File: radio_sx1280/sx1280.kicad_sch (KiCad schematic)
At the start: 5 parts

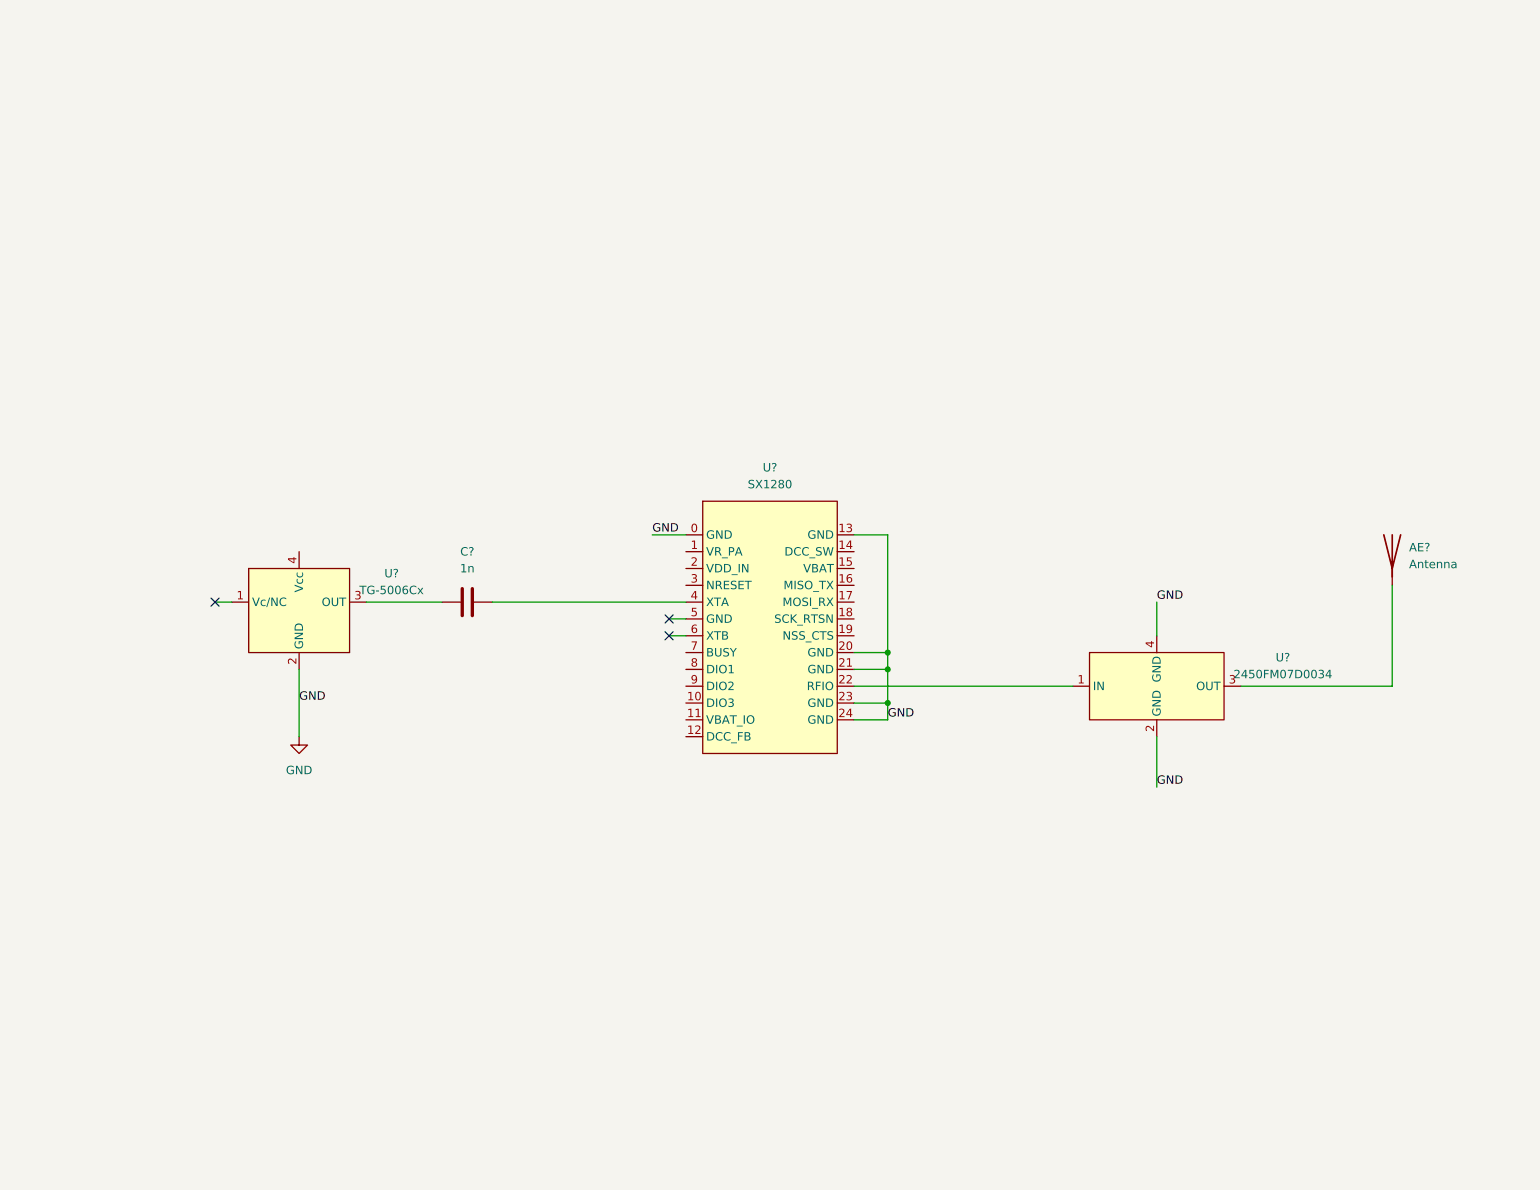
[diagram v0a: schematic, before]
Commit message: schematic capture complete
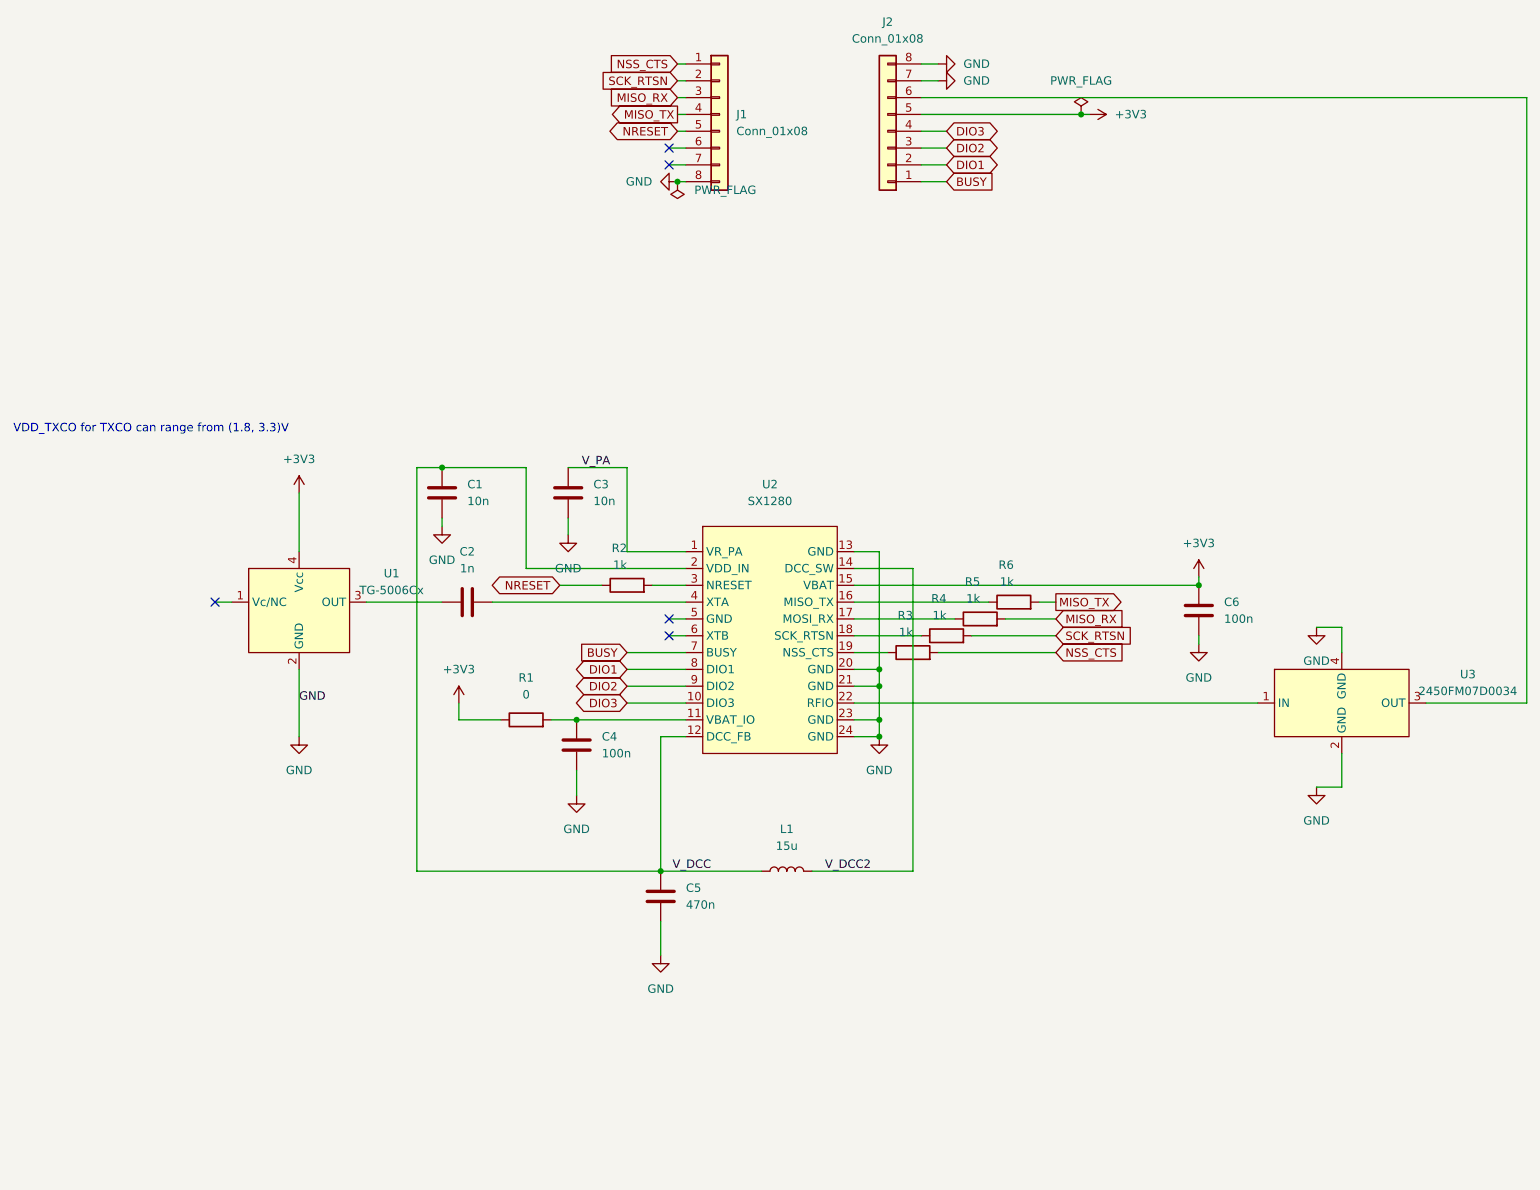
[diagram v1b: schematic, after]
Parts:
- removed AE?: Antenna, symbol Device:Antenna
- added C1, C3: 10n, symbol Device:C
- added C4, C6: 100n, symbol Device:C
- added C5: 470n, symbol Device:C
- added J1, J2: Conn_01x08, symbol Connector_Generic:Conn_01x08
- added L1: 15u, symbol Device:L
- added R1: 0, symbol Device:R
- added R2, R3, R4, R5, R6: 1k, symbol Device:R
- gave numbers to parts that had none: 4
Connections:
- net GND: now also C1.2, C3.2, C4.2, C5.2, C6.2, J1.8 (Pin_8), J2.7 (Pin_7), J2.8 (Pin_8); no longer U2.0 (GND)
- net V_PA: now reaches U2.1 (VR_PA)
- net V_PA: now also C3.1
- net DIO3: now reaches U2.10 (DIO3)
- net DIO3: now also J2.4 (Pin_4)
- net at U2.11 (VBAT_IO): now also C4.1, R1.2
- net V_DCC: now reaches U2.12 (DCC_FB)
- net V_DCC: now also U2.2 (VDD_IN), C1.1, C5.1, L1.1
- net V_DCC2: now reaches U2.14 (DCC_SW)
- net V_DCC2: now also L1.2
- net +3V3: now reaches U2.15 (VBAT)
- net +3V3: now also U1.4 (Vcc), C6.1, J2.5 (Pin_5), R1.1
- net at U2.16 (MISO_TX): now also R6.1
- net at U2.17 (MOSI_RX): now also R5.1
- net at U2.18 (SCK_RTSN): now also R4.1
- net at U2.19 (NSS_CTS): now also R3.1
- net at U2.3 (NRESET): now also R2.2
- net BUSY: now reaches U2.7 (BUSY)
- net BUSY: now also J2.1 (Pin_1)
- net DIO1: now reaches U2.8 (DIO1)
- net DIO1: now also J2.2 (Pin_2)
- net DIO2: now reaches U2.9 (DIO2)
- net DIO2: now also J2.3 (Pin_3)
- net at U3.3 (OUT): now also J2.6 (Pin_6)
- new net MISO_RX: J1.3 (Pin_3), R5.2
- new net MISO_TX: J1.4 (Pin_4), R6.2
- new net NRESET: J1.5 (Pin_5), R2.1
- new net NSS_CTS: J1.1 (Pin_1), R3.2
- new net SCK_RTSN: J1.2 (Pin_2), R4.2
- no-connect marks 3 -> 5
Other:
- note added: "VDD_TXCO for TXCO can range from (1.8, 3.3)V"
- moved on the sheet: U3

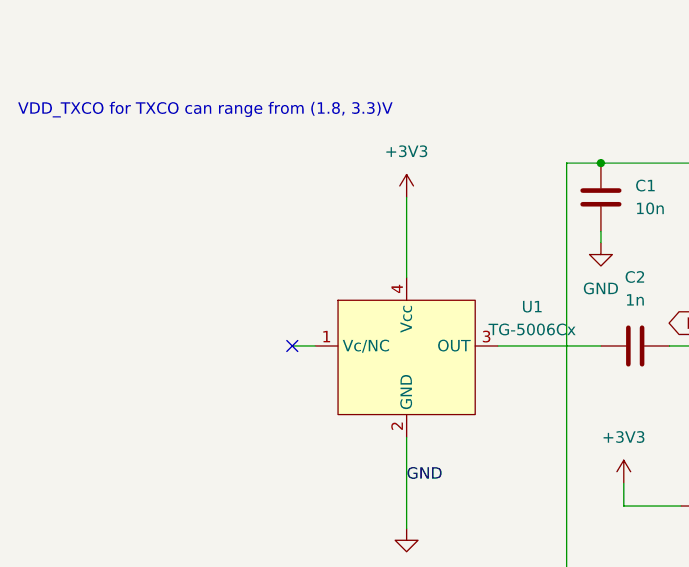
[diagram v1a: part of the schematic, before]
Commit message: add decoupling cap to txco vdd
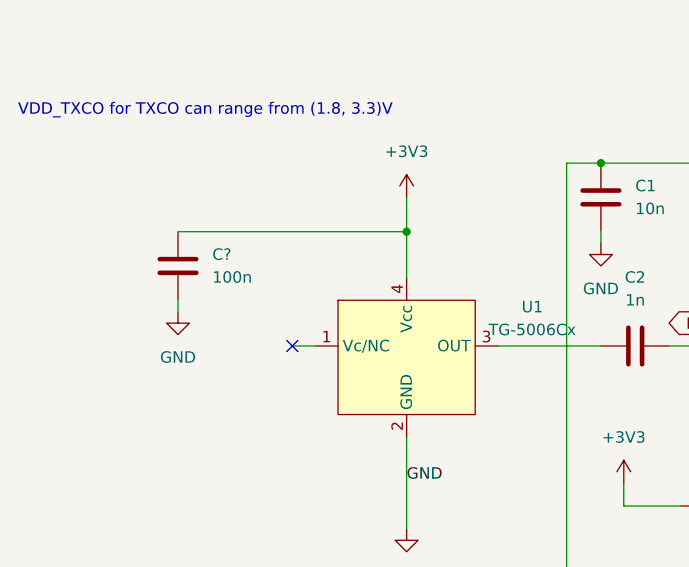
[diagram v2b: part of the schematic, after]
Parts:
- added C?: 100n, symbol Device:C
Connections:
- net +3V3: now also C?.1
- net GND: now also C?.2
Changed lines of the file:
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@@
 (kicad_sch (version 20211123) (generator eeschema)
   (paper "A4")
+  (junction (at 76.2 91.44) (diameter 0) (color 0 0 0 0)
+  )
   (junction (at 163.83 121.92) (diameter 0) (color 0 0 0 0)
   )
@@
     (stroke (width 0) (type default) (color 0 0 0 0))
   )
+  (wire (pts (xy 50.8 91.44) (xy 76.2 91.44))
+    (stroke (width 0) (type default) (color 0 0 0 0))
+  )
   (wire (pts (xy 86.36 104.14) (xy 97.79 104.14))
     (stroke (width 0) (type default) (color 0 0 0 0))
@@
     (stroke (width 0) (type default) (color 0 0 0 0))
   )
-  (wire (pts (xy 76.2 87.63) (xy 76.2 96.52))
+  (wire (pts (xy 76.2 87.63) (xy 76.2 91.44))
     (stroke (width 0) (type default) (color 0 0 0 0))
   )
@@
     (stroke (width 0) (type default) (color 0 0 0 0))
   )
+  (wire (pts (xy 76.2 91.44) (xy 76.2 96.52))
+    (stroke (width 0) (type default) (color 0 0 0 0))
+  )
   (wire (pts (xy 163.83 116.84) (xy 163.83 121.92))
     (stroke (width 0) (type default) (color 0 0 0 0))
@@
   )
   (wire (pts (xy 160.02 121.92) (xy 163.83 121.92))
+    (stroke (width 0) (type default) (color 0 0 0 0))
+  )
+  (wire (pts (xy 50.8 99.06) (xy 50.8 100.33))
     (stroke (width 0) (type default) (color 0 0 0 0))
   )
@@
     )
   )
+  (symbol (lib_id "Device:C") (at 50.8 95.25 0) (unit 1)
+    (in_bom yes) (on_board yes) (fields_autoplaced)
+    (property "Reference" "C?" (id 0) (at 54.61 93.9799 0)
+      (effects (font (size 1.27 1.27)) (justify left))
+    )
+    (property "Value" "100n" (id 1) (at 54.61 96.5199 0)
+      (effects (font (size 1.27 1.27)) (justify left))
+    )
+    (property "Footprint" "" (id 2) (at 51.7652 99.06 0)
+      (effects (font (size 1.27 1.27)) hide)
+    )
+    (property "Datasheet" "~" (id 3) (at 50.8 95.25 0)
+      (effects (font (size 1.27 1.27)) hide)
+    )
+    (pin "1")
+    (pin "2")
+  )
   (symbol (lib_id "Device:R") (at 110.49 121.92 90) (unit 1)
     (in_bom yes) (on_board yes) (fields_autoplaced)
@@
     )
     (property "Datasheet" "" (id 3) (at 172.72 22.86 0)
+      (effects (font (size 1.27 1.27)) hide)
+    )
+    (pin "1")
+  )
+  (symbol (lib_id "power:GND") (at 50.8 100.33 0) (unit 1)
+    (in_bom yes) (on_board yes) (fields_autoplaced)
+    (property "Reference" "#PWR?" (id 0) (at 50.8 106.68 0)
+      (effects (font (size 1.27 1.27)) hide)
+    )
+    (property "Value" "GND" (id 1) (at 50.8 105.41 0))
+    (property "Footprint" "" (id 2) (at 50.8 100.33 0)
+      (effects (font (size 1.27 1.27)) hide)
+    )
+    (property "Datasheet" "" (id 3) (at 50.8 100.33 0)
       (effects (font (size 1.27 1.27)) hide)
     )
@@
       (reference "#PWR016") (unit 1) (value "GND") (footprint "")
     )
+    (path "/111c38f7-ec2b-444f-8ec0-61814dc6a219"
+      (reference "#PWR?") (unit 1) (value "GND") (footprint "")
+    )
     (path "/47782e64-2d17-4f99-a0cc-f4579b8e511b"
       (reference "C1") (unit 1) (value "10n") (footprint "")
@@
       (reference "C6") (unit 1) (value "100n") (footprint "")
     )
+    (path "/03542ce4-c372-4a46-bc37-431855927029"
+      (reference "C?") (unit 1) (value "100n") (footprint "")
+    )
     (path "/71ce0edd-2fca-4e62-aacd-1e2fc34784e5"
